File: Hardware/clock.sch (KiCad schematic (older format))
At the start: 49 parts, among them J1 Conn_02x05_Counter_Clockwise, J2 Conn_01x02_Male, J3 USB_B_Micro, J4 Barrel_Jack, Q1 2N7002ET1G, SW1 SW_Push, SW2 SW_Push, SW3 SW_Push, U1 STM32F103C8Tx, U2 UA78M33CDCY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

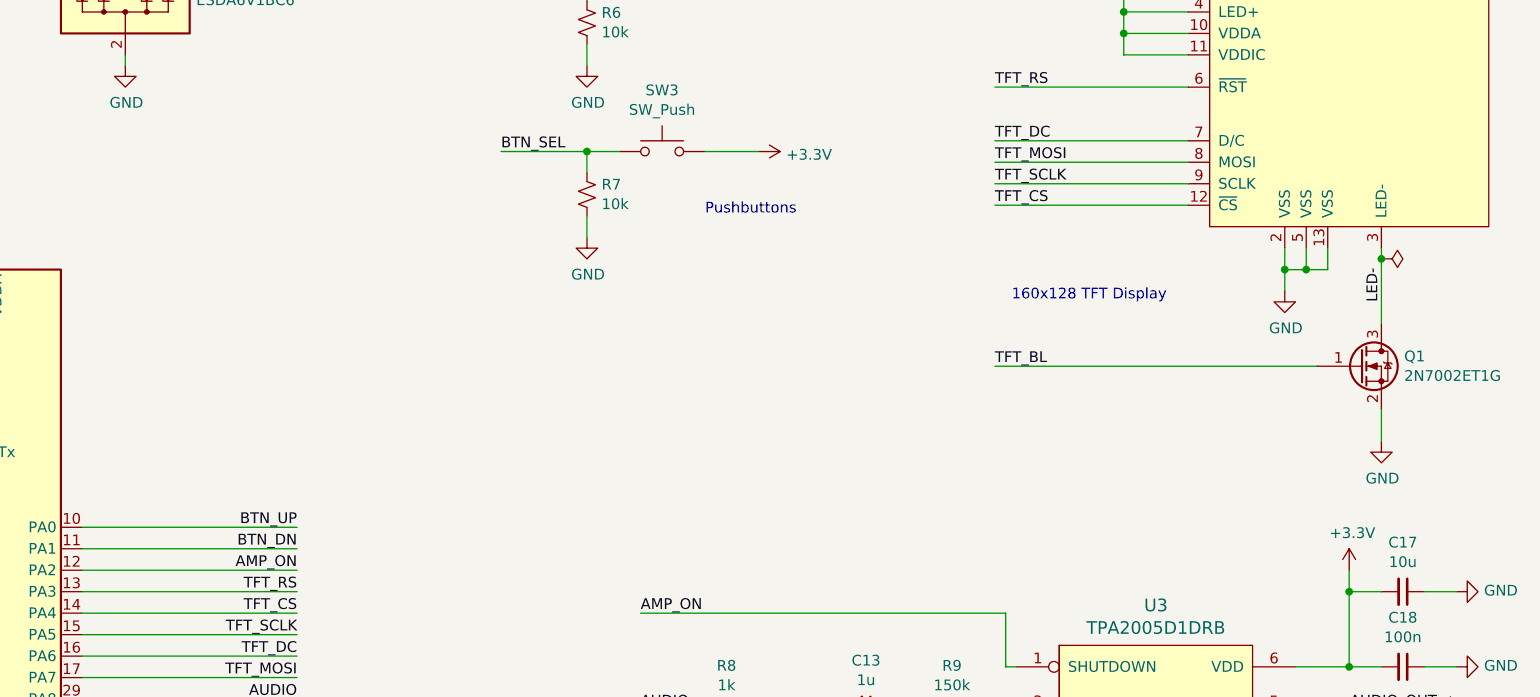
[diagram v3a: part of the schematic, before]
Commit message: Added filter for amplifier supply. Some routing.
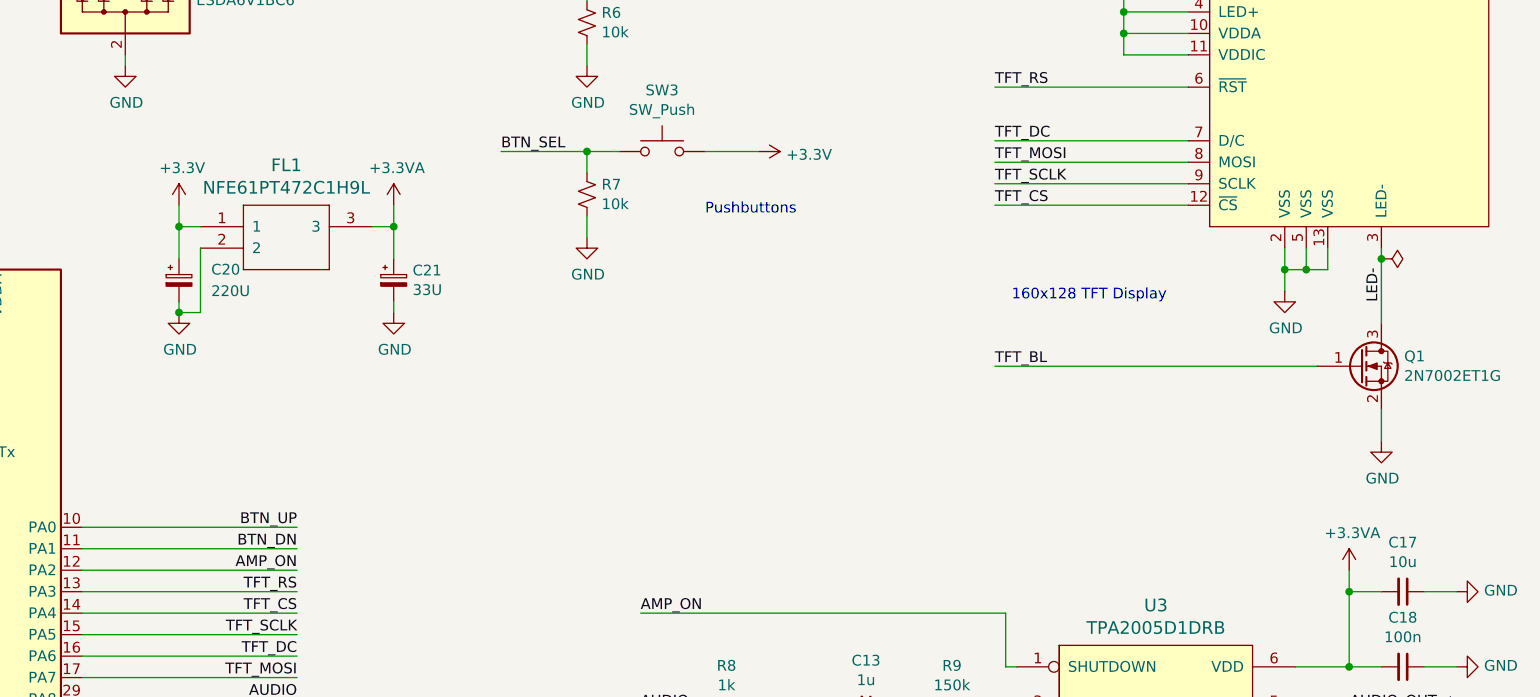
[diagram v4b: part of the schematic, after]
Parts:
- added C20: 220U, Capacitor_Tantalum_SMD:CP_EIA-7343-20_Kemet-V_Pad2.25x2.55mm_HandSolder, symbol Device:CP_Small
- added C21: 33U, Capacitor_Tantalum_SMD:CP_EIA-3528-21_Kemet-B_Pad1.50x2.35mm_HandSolder, symbol Device:CP_Small
- added FL1: NFE61PT472C1H9L, Footprints:6816, symbol nfe61pt472c1h9l:NFE61PT472C1H9L
- C17: footprint Capacitor_SMD:C_0603_1608Metric_Pad1.05x0.95mm_HandSolder -> Capacitor_SMD:C_0402_1005Metric
- J4: footprint Foodprints:PJ-102A -> Footprints:PJ-102A
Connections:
- net +3V3: now also C20.1, FL1.1; no longer C17.2, C18.2, U3.6 (VDD)
- net GND: now also C20.2, C21.2, FL1.2
- new net +3.3VA: C17.2, C18.2, C21.1, FL1.3, U3.6 (VDD)
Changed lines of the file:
@@
 Text Label 6800 4800 0    50   ~ 0
 AMP_ON
-$Comp
-L power:+3.3V #PWR0103
-U 1 1 5E2E1699
-P 10100 4600
-F 0 "#PWR0103" H 10100 4450 50  0001 C CNN
-F 1 "+3.3V" H 10115 4773 50  0000 C CNN
-F 2 "" H 10100 4600 50  0001 C CNN
-F 3 "" H 10100 4600 50  0001 C CNN
-	1    10100 4600
-	1    0    0    -1
-$EndComp
 Wire Wire Line
 	10100 5050 9850 5050
@@
 F 0 "C17" V 10121 4700 50  0000 C CNN
 F 1 "10u" V 10212 4700 50  0000 C CNN
-F 2 "Capacitor_SMD:C_0603_1608Metric_Pad1.05x0.95mm_HandSolder" H 10350 4700 50  0001 C CNN
+F 2 "Capacitor_SMD:C_0402_1005Metric" H 10350 4700 50  0001 C CNN
 F 3 "~" H 10350 4700 50  0001 C CNN
 	1    10350 4700
@@
 F 0 "J4" H 4970 1204 50  0000 R CNN
 F 1 "Barrel_Jack" H 4970 1159 50  0001 R CNN
-F 2 "Foodprints:PJ-102A" H 5250 1160 50  0001 C CNN
+F 2 "Footprints:PJ-102A" H 5250 1160 50  0001 C CNN
 F 3 "~" H 5250 1160 50  0001 C CNN
 	1    5200 1200
@@
 Wire Wire Line
 	4200 1350 4600 1350
+$Comp
+L nfe61pt472c1h9l:NFE61PT472C1H9L FL1
+U 1 1 5E7C3083
+P 4750 3000
+F 0 "FL1" H 5150 3286 59  0000 C CNN
+F 1 "NFE61PT472C1H9L" H 5150 3181 59  0000 C CNN
+F 2 "Footprints:6816" H 4750 3000 50  0001 C CNN
+F 3 "" H 4750 3000 50  0001 C CNN
+	1    4750 3000
+	1    0    0    -1
+$EndComp
+$Comp
+L power:GND #PWR02
+U 1 1 5E7C51A7
+P 4650 3400
+F 0 "#PWR02" H 4650 3150 50  0001 C CNN
+F 1 "GND" H 4655 3227 50  0000 C CNN
+F 2 "" H 4650 3400 50  0001 C CNN
+F 3 "" H 4650 3400 50  0001 C CNN
+	1    4650 3400
+	1    0    0    -1
+$EndComp
+$Comp
+L power:+3.3V #PWR01
+U 1 1 5E7D138A
+P 4650 2900
+F 0 "#PWR01" H 4650 2750 50  0001 C CNN
+F 1 "+3.3V" H 4665 3073 50  0000 C CNN
+F 2 "" H 4650 2900 50  0001 C CNN
+F 3 "" H 4650 2900 50  0001 C CNN
+	1    4650 2900
+	1    0    0    -1
+$EndComp
+Wire Wire Line
+	4750 3000 4650 3000
+Wire Wire Line
+	4650 3000 4650 2900
+$Comp
+L power:+3.3VA #PWR03
+U 1 1 5E7DDB4E
+P 5650 2900
+F 0 "#PWR03" H 5650 2750 50  0001 C CNN
+F 1 "+3.3VA" H 5665 3073 50  0000 C CNN
+F 2 "" H 5650 2900 50  0001 C CNN
+F 3 "" H 5650 2900 50  0001 C CNN
+	1    5650 2900
+	1    0    0    -1
+$EndComp
+$Comp
+L Device:CP_Small C20
+U 1 1 5E7EB531
+P 4650 3250
+F 0 "C20" H 4800 3300 50  0000 L CNN
+F 1 "220U" H 4800 3200 50  0000 L CNN
+F 2 "Capacitor_Tantalum_SMD:CP_EIA-7343-20_Kemet-V_Pad2.25x2.55mm_HandSolder" H 4650 3250 50  0001 C CNN
+F 3 "~" H 4650 3250 50  0001 C CNN
+	1    4650 3250
+	1    0    0    -1
+$EndComp
+$Comp
+L Device:CP_Small C21
+U 1 1 5E7ED9A9
+P 5650 3250
+F 0 "C21" H 5738 3296 50  0000 L CNN
+F 1 "33U" H 5738 3205 50  0000 L CNN
+F 2 "Capacitor_Tantalum_SMD:CP_EIA-3528-21_Kemet-B_Pad1.50x2.35mm_HandSolder" H 5650 3250 50  0001 C CNN
+F 3 "~" H 5650 3250 50  0001 C CNN
+	1    5650 3250
+	1    0    0    -1
+$EndComp
+Wire Wire Line
+	5650 2900 5650 3000
+Wire Wire Line
+	5550 3000 5650 3000
+Connection ~ 5650 3000
+Wire Wire Line
+	5650 3000 5650 3150
+Wire Wire Line
+	4650 3150 4650 3000
+Connection ~ 4650 3000
+$Comp
+L power:GND #PWR04
+U 1 1 5E814825
+P 5650 3400
+F 0 "#PWR04" H 5650 3150 50  0001 C CNN
+F 1 "GND" H 5655 3227 50  0000 C CNN
+F 2 "" H 5650 3400 50  0001 C CNN
+F 3 "" H 5650 3400 50  0001 C CNN
+	1    5650 3400
+	1    0    0    -1
+$EndComp
+Wire Wire Line
+	4650 3400 4650 3350
+Wire Wire Line
+	5650 3400 5650 3350
+Wire Wire Line
+	4750 3100 4750 3400
+Wire Wire Line
+	4750 3400 4650 3400
+Connection ~ 4650 3400
+$Comp
+L power:+3.3VA #PWR?
+U 1 1 5E859AF1
+P 10100 4600
+F 0 "#PWR?" H 10100 4450 50  0001 C CNN
+F 1 "+3.3VA" H 10115 4773 50  0000 C CNN
+F 2 "" H 10100 4600 50  0001 C CNN
+F 3 "" H 10100 4600 50  0001 C CNN
+	1    10100 4600
+	1    0    0    -1
+$EndComp
 $EndSCHEMATC

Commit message: Routing complete
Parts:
- added R11: 100R, Resistor_SMD:R_0603_1608Metric, symbol Device:R_Small_US
- J4: footprint Footprints:PJ-102A -> Footprints:DC-005-SMT
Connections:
- net TFT_BL: now also R11.1; no longer Q1.1 (G)
- new net: Q1.1 (G), R11.2
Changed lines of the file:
@@
 Wire Wire Line
 	10250 3100 10250 3150
-Wire Wire Line
-	8450 3650 9950 3650
 Text Label 8450 3650 0    50   ~ 0
 TFT_BL
@@
 F 0 "J4" H 4970 1204 50  0000 R CNN
 F 1 "Barrel_Jack" H 4970 1159 50  0001 R CNN
-F 2 "Footprints:PJ-102A" H 5250 1160 50  0001 C CNN
+F 2 "Footprints:DC-005-SMT" H 5250 1160 50  0001 C CNN
 F 3 "~" H 5250 1160 50  0001 C CNN
 	1    5200 1200
@@
 Connection ~ 4650 3400
 $Comp
-L power:+3.3VA #PWR?
+L power:+3.3VA #PWR05
 U 1 1 5E859AF1
 P 10100 4600
-F 0 "#PWR?" H 10100 4450 50  0001 C CNN
+F 0 "#PWR05" H 10100 4450 50  0001 C CNN
 F 1 "+3.3VA" H 10115 4773 50  0000 C CNN
 F 2 "" H 10100 4600 50  0001 C CNN
@@
 	1    0    0    -1
 $EndComp
+$Comp
+L Device:R_Small_US R11
+U 1 1 5E72A806
+P 9400 3650
+F 0 "R11" H 9332 3604 50  0000 R CNN
+F 1 "100R" H 9332 3695 50  0000 R CNN
+F 2 "Resistor_SMD:R_0603_1608Metric" H 9400 3650 50  0001 C CNN
+F 3 "~" H 9400 3650 50  0001 C CNN
+	1    9400 3650
+	0    -1   -1   0
+$EndComp
+Wire Wire Line
+	9950 3650 9500 3650
+Wire Wire Line
+	9300 3650 8450 3650
 $EndSCHEMATC

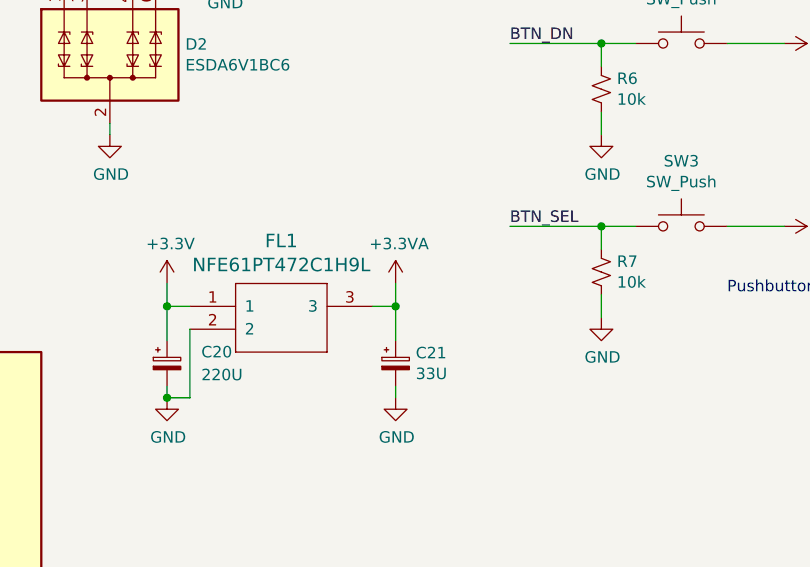
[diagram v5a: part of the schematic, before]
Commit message: Added FreeCAD model of enclosure + PCB. Small changes to PCB layout. Added STEP model of TFT display.
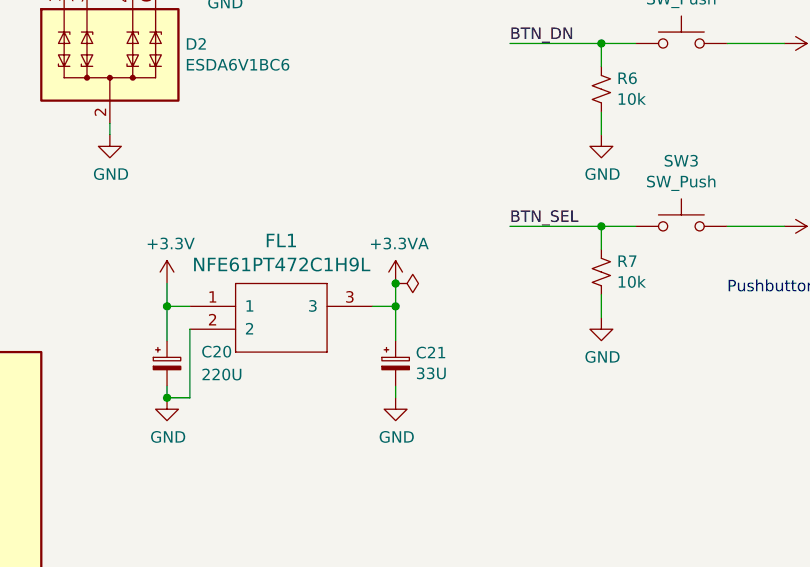
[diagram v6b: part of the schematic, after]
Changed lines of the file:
@@
 Wire Wire Line
 	9300 3650 8450 3650
+$Comp
+L power:PWR_FLAG #FLG0104
+U 1 1 5E7F3002
+P 5650 2900
+F 0 "#FLG0104" H 5650 2975 50  0001 C CNN
+F 1 "PWR_FLAG" V 5650 3028 50  0001 L CNN
+F 2 "" H 5650 2900 50  0001 C CNN
+F 3 "~" H 5650 2900 50  0001 C CNN
+	1    5650 2900
+	0    1    1    0
+$EndComp
+Connection ~ 5650 2900
 $EndSCHEMATC
